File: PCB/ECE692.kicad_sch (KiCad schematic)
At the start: 16 parts, among them J1 TYPE-C_16PIN_2MD__073_, J2 Conn_01x12, J3 Screw_Terminal_01x02, J4 Screw_Terminal_01x02, U1 CAN_BUS_TRANSCEIVER1, U2 CAN_BUS_TRANSCEIVER2, U4 STM32F446RETx, U5 LEVEL_SHIFTER

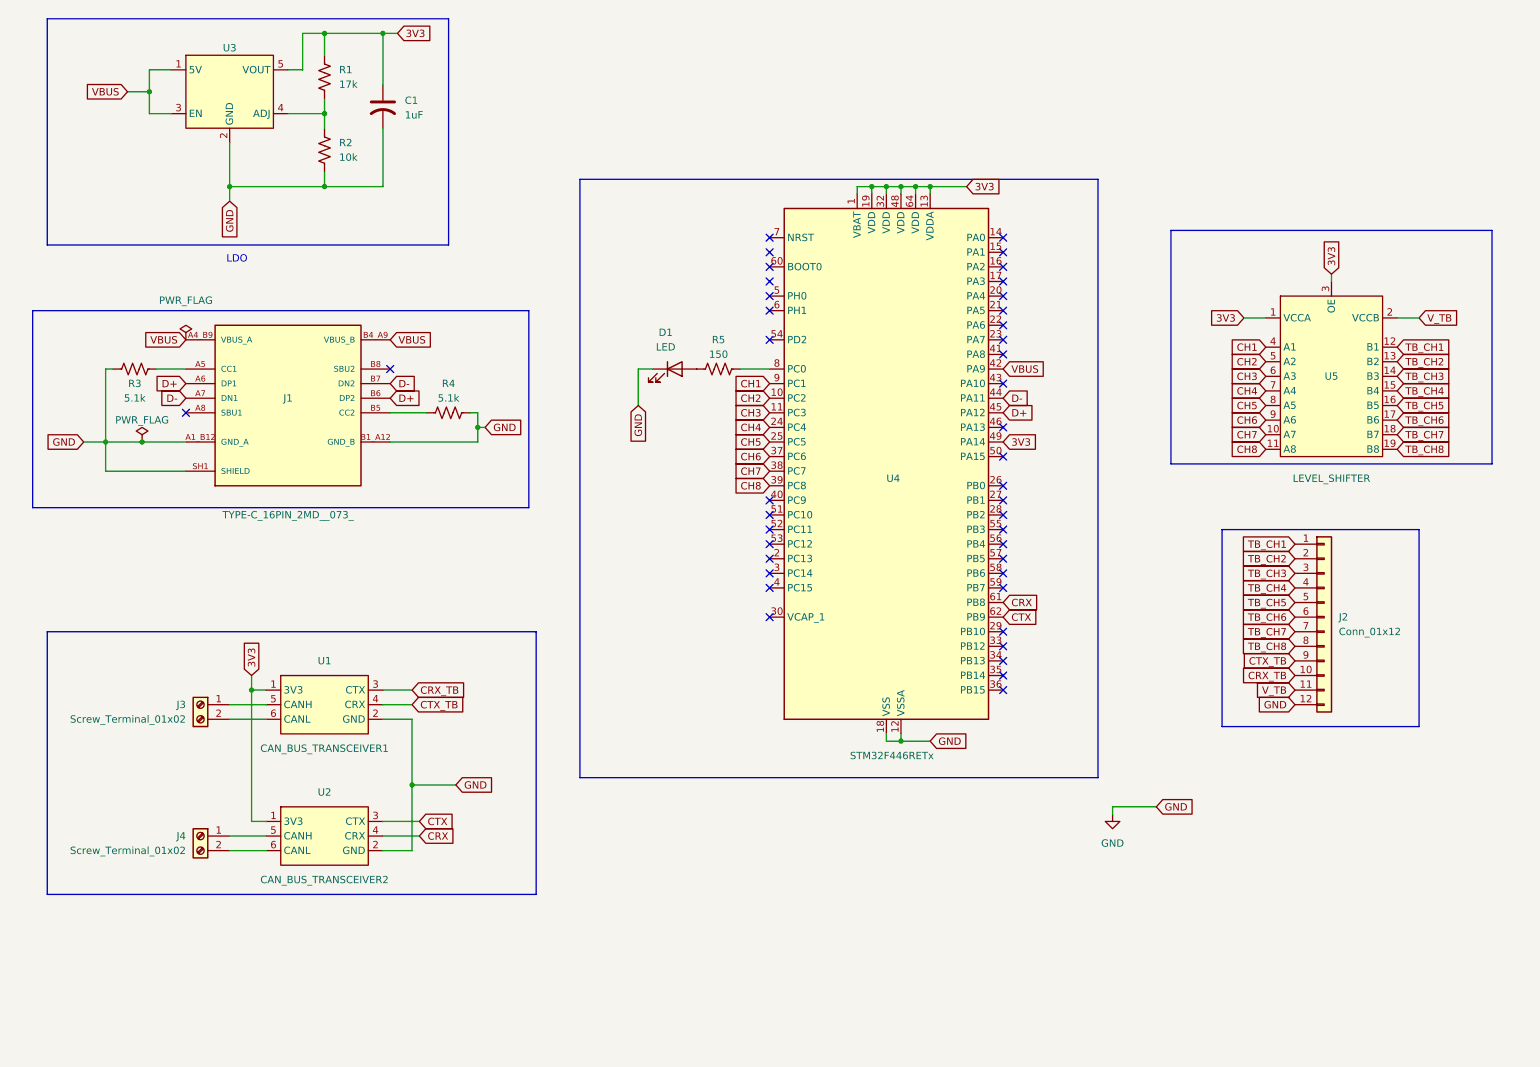
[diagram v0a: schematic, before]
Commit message: Modified some stuff, and did some routing
- Replaced the rectangle with the STM nucleo board shape
- added the level shifter symbol and footprint
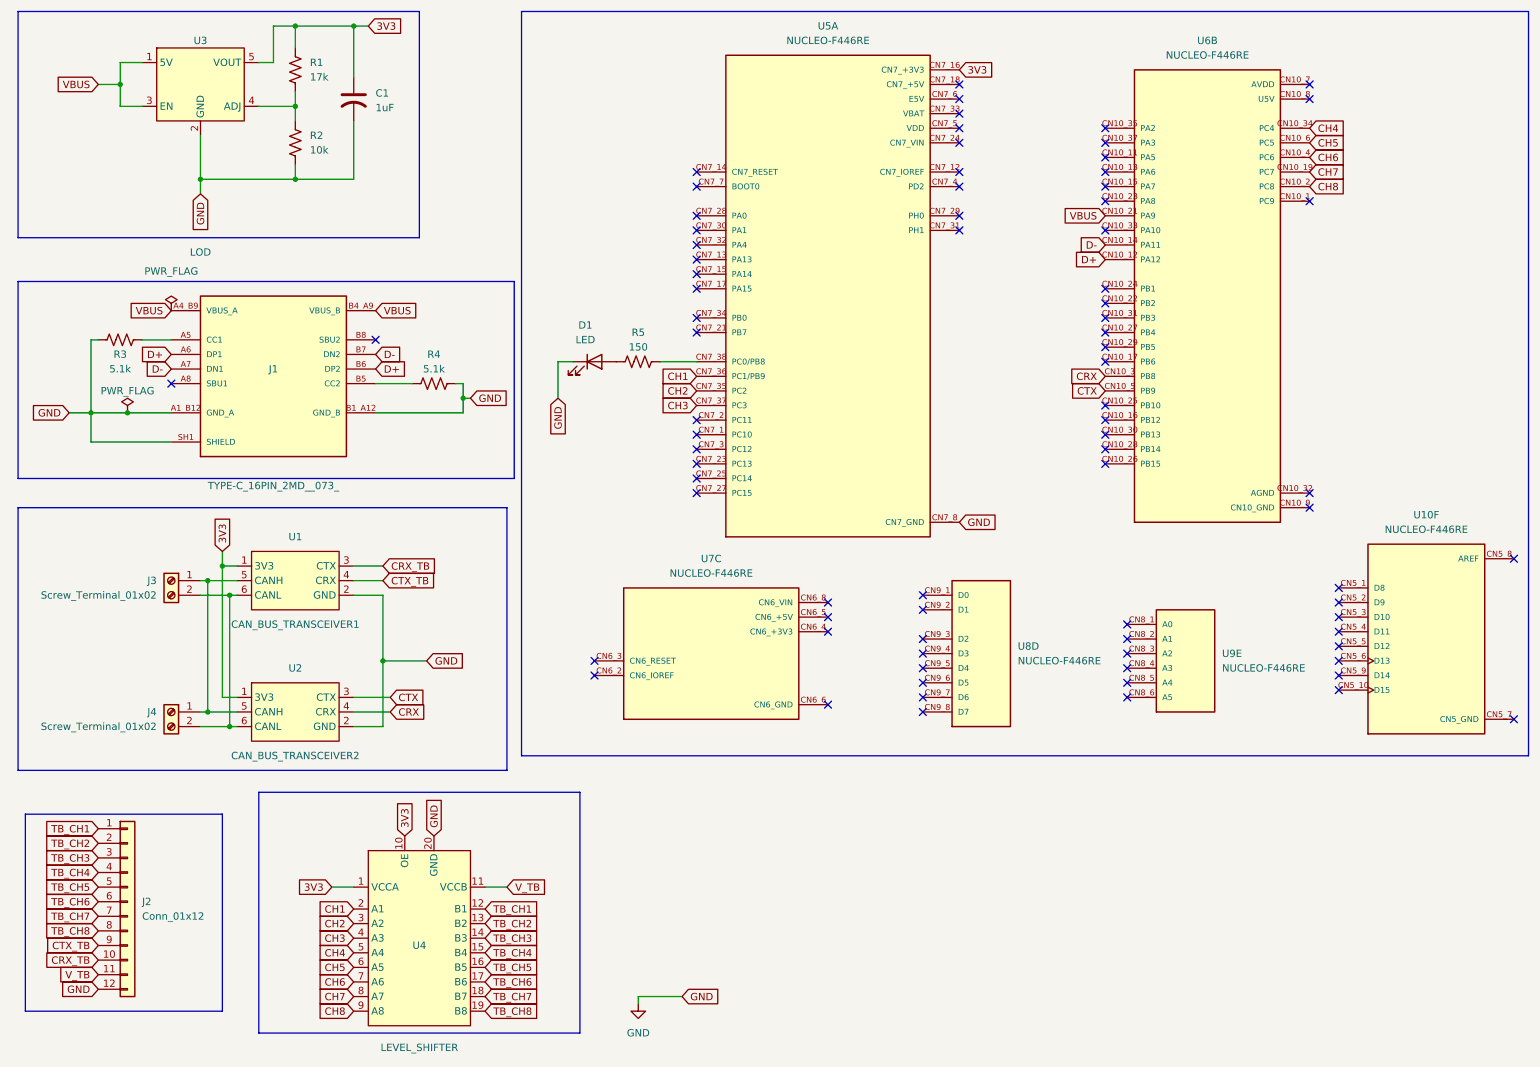
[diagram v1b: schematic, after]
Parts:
- removed U4: STM32F446RETx, Package_QFP:LQFP-64_10x10mm_P0.5mm, symbol MCU_ST_STM32F4:STM32F446RETx
- added U10, U5, U6, U7, U8, U9: NUCLEO-F446RE, NUCLEO-F446RE:MODULE_NUCLEO-F446RE, symbol NUCLEO-F446RE:NUCLEO-F446RE
- U3: value (none) -> LOD
- U4: renamed from U5; footprint (none) -> footprints:LEVEL_SHIFTER
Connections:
- net 3V3: now also U4.10 (OE), U5.CN7_16 (CN7_+3V3); no longer U4.3 (OE)
- net CH1: now also U4.2 (A1), U5.CN7_36 (PC1/PB9); no longer U4.4 (A1)
- net CH2: now also U4.3 (A2), U5.CN7_35 (PC2); no longer U4.5 (A2)
- net CH3: now also U4.4 (A3), U5.CN7_37 (PC3); no longer U4.6 (A3)
- net CH4: now also U4.5 (A4), U6.CN10_34 (PC4); no longer U4.7 (A4)
- net CH5: now also U4.6 (A5), U6.CN10_6 (PC5); no longer U4.8 (A5)
- net CH6: now also U4.7 (A6), U6.CN10_4 (PC6); no longer U4.9 (A6)
- net CH7: now also U4.8 (A7), U6.CN10_19 (PC7); no longer U4.10 (A7)
- net CH8: now also U4.9 (A8), U6.CN10_2 (PC8); no longer U4.11 (A8)
- net CRX: now also U6.CN10_3 (PB8)
- net CTX: now also U6.CN10_5 (PB9)
- net D+: now also U6.CN10_12 (PA12)
- net D-: now also U6.CN10_14 (PA11)
- net VBUS: now also U6.CN10_21 (PA9)
- net V_TB: now also U4.11 (VCCB); no longer U4.2 (VCCB)
- net at R5.2: now also U5.CN7_38 (PC0/PB8)
- net at J4.1 (Pin_1), U2.5 (CANH): now also J3.1 (Pin_1), U1.5 (CANH)
- net at J4.2 (Pin_2), U2.6 (CANL): now also J3.2 (Pin_2), U1.6 (CANL)
- net GND renamed CN7_GND
- net CN7_GND: now also U4.20 (GND), U5.CN7_19 (CN7_GND), U5.CN7_20 (CN7_GND), U5.CN7_22 (CN7_GND), U5.CN7_8 (CN7_GND)
- new net CN10_GND: U6.CN10_20 (CN10_GND), U6.CN10_9 (CN10_GND)
- new net CN6_GND: U7.CN6_6 (CN6_GND), U7.CN6_7 (CN6_GND)
- no-connect marks 42 -> 80
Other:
- note removed: "LDO"
- moved on the sheet: C1, D1, J1, J2, J3, J4, R1, R2, R3, R4, R5, U1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

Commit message: Finished the PCB
- Finished the PCB and ordered at JLCPCB
- Uploaded schematic pdf, and image of complete layout and routing
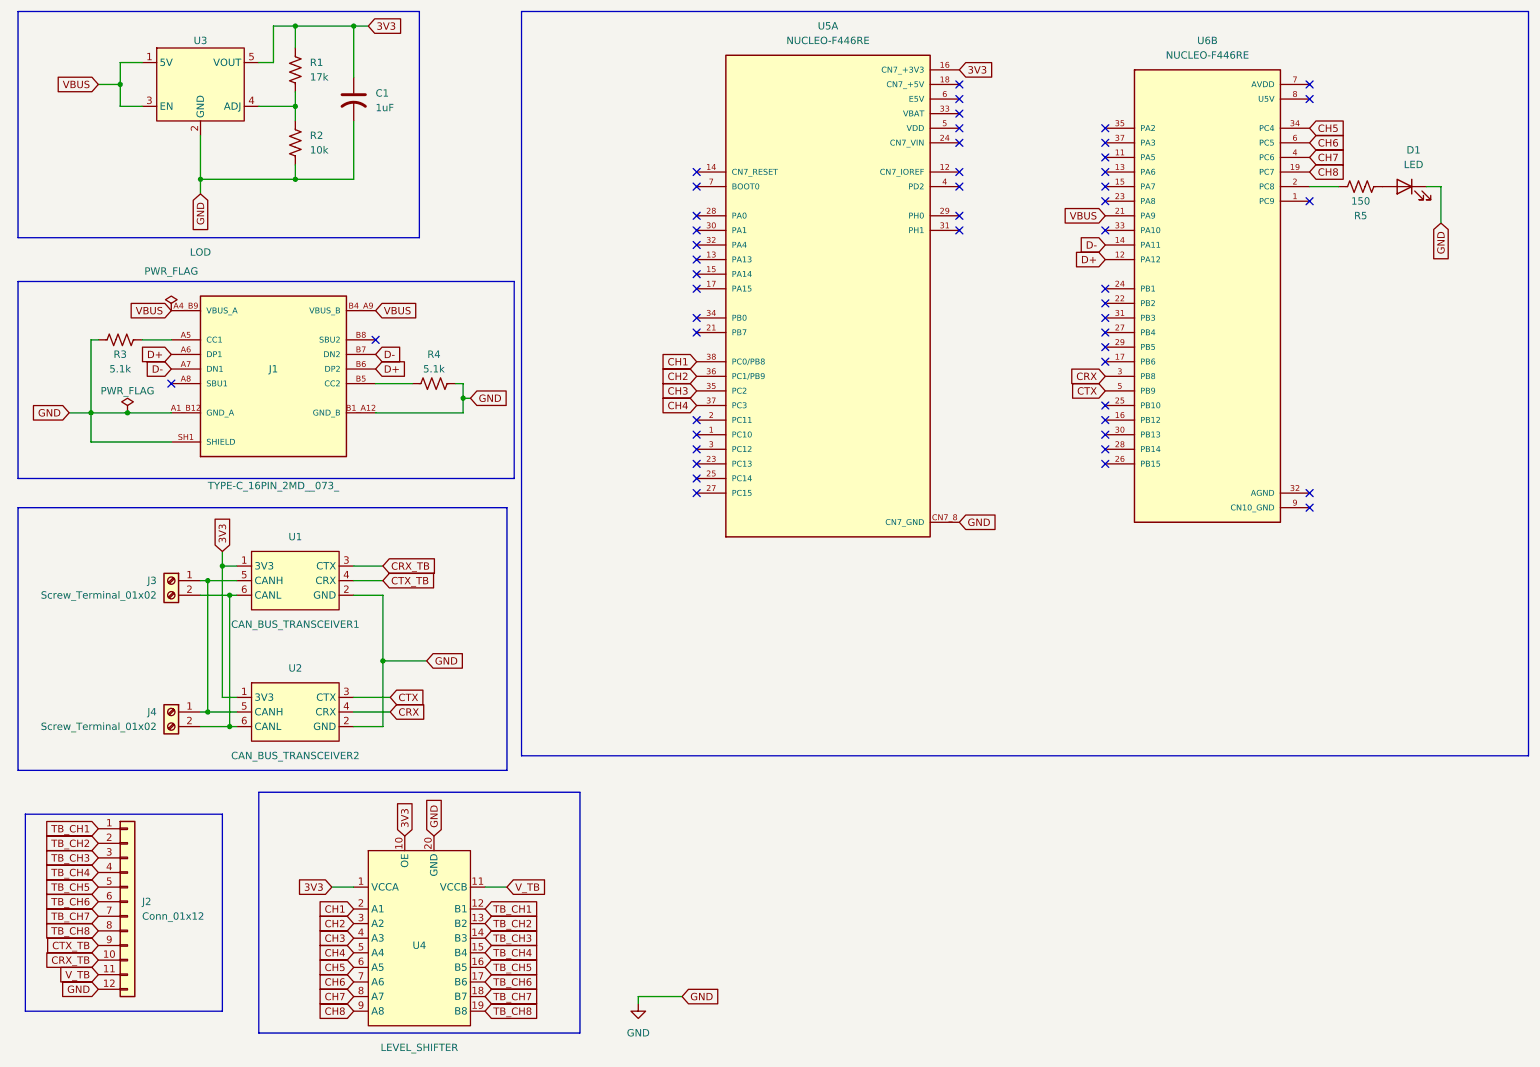
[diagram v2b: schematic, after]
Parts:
- removed U10, U7, U8, U9: NUCLEO-F446RE, NUCLEO-F446RE:MODULE_NUCLEO-F446RE, symbol NUCLEO-F446RE:NUCLEO-F446RE
- U5, U6: footprint NUCLEO-F446RE:MODULE_NUCLEO-F446RE -> Connector_PinHeader_2.54mm:PinHeader_2x19_P2.54mm_Vertical
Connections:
- net 3V3: now also U5.16 (CN7_+3V3); no longer U5.CN7_16 (CN7_+3V3)
- net CH1: now also U5.38 (PC0/PB8); no longer U5.CN7_36 (PC1/PB9)
- net CH2: now also U5.36 (PC1/PB9); no longer U5.CN7_35 (PC2)
- net CH3: now also U5.35 (PC2); no longer U5.CN7_37 (PC3)
- net CH4: now also U5.37 (PC3); no longer U6.CN10_34 (PC4)
- net CH5: now also U6.34 (PC4); no longer U6.CN10_6 (PC5)
- net CH6: now also U6.6 (PC5); no longer U6.CN10_4 (PC6)
- net CH7: now also U6.4 (PC6); no longer U6.CN10_19 (PC7)
- net CH8: now also U6.19 (PC7); no longer U6.CN10_2 (PC8)
- net CN10_GND: now also U6.9 (CN10_GND); no longer U6.CN10_9 (CN10_GND)
- net CRX: now also U6.3 (PB8); no longer U6.CN10_3 (PB8)
- net CTX: now also U6.5 (PB9); no longer U6.CN10_5 (PB9)
- net D+: now also U6.12 (PA12); no longer U6.CN10_12 (PA12)
- net D-: now also U6.14 (PA11); no longer U6.CN10_14 (PA11)
- net VBUS: now also U6.21 (PA9); no longer U6.CN10_21 (PA9)
- net at R5.2: now also U6.2 (PC8); no longer U5.CN7_38 (PC0/PB8)
- no-connect marks 80 -> 50
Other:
- moved on the sheet: D1, R5
